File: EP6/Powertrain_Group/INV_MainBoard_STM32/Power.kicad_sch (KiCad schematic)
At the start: 42 parts, among them J3 LVBattery, U2 TPS5430DDA, U3 AMS1117-3.3

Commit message: Inverter board adjust
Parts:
- D3, D5: footprint Diode_SMD:D_SMB -> Diode_SMD:D_SOD-323
- U2: value TPS5430DDA -> TPS5430DDAR
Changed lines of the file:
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@@
 			)
 		)
-		(property "Footprint" "Diode_SMD:D_SMB"
+		(property "Footprint" "Diode_SMD:D_SOD-323"
 			(at 240.03 44.45 90)
 			(effects
@@
 			)
 		)
-		(property "Value" "TPS5430DDA"
+		(property "Value" "TPS5430DDAR"
 			(at 137.16 81.28 0)
 			(effects
@@
 			)
 		)
-		(property "Footprint" "Diode_SMD:D_SMB"
+		(property "Footprint" "Diode_SMD:D_SOD-323"
 			(at 264.16 93.98 90)
 			(effects

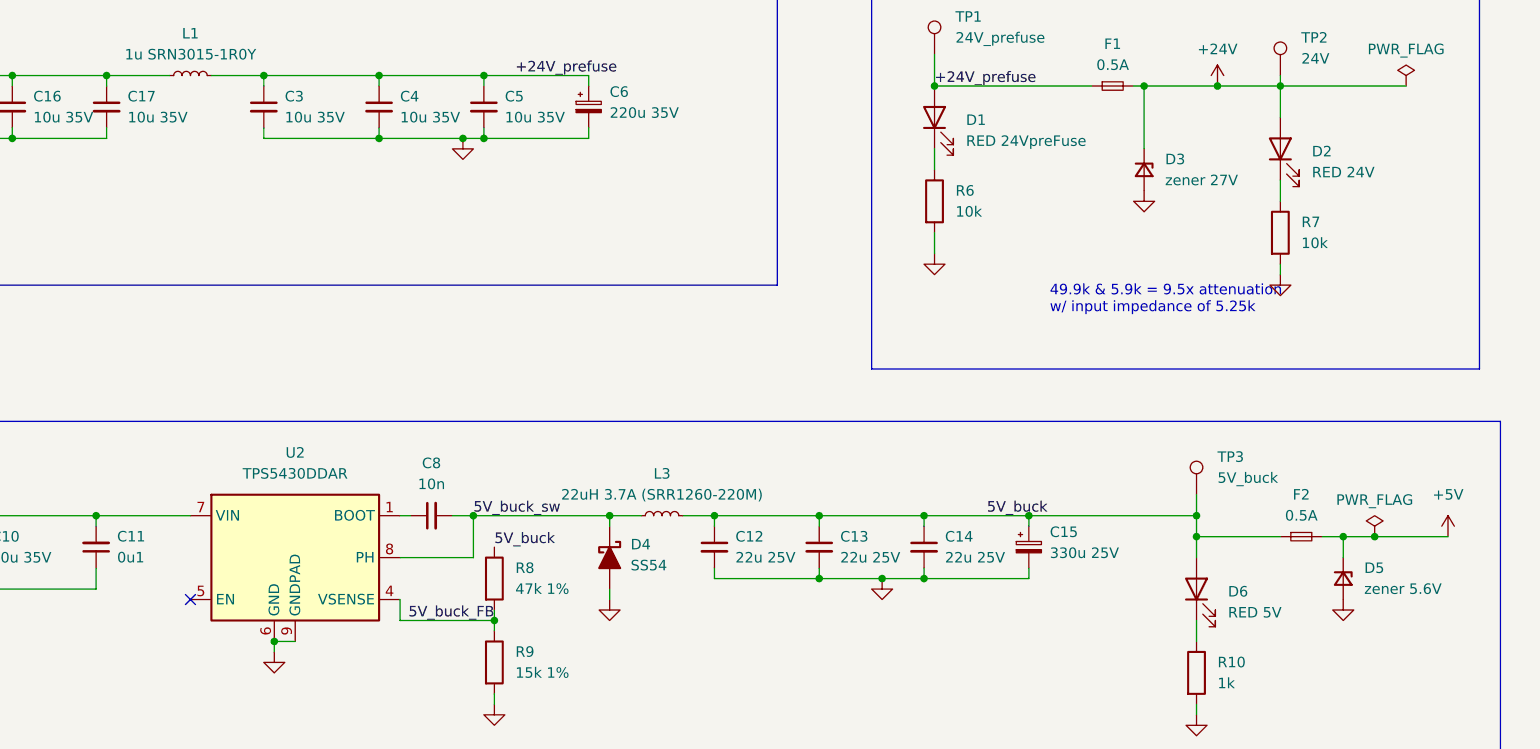
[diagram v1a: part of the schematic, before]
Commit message: batch update for JLCPCB 241117
6SBMS
ACC_HVLV1
INV_CurrentSense2
INV_CurrentSense3
DClinkCap1
INV_MainBoard_STM32
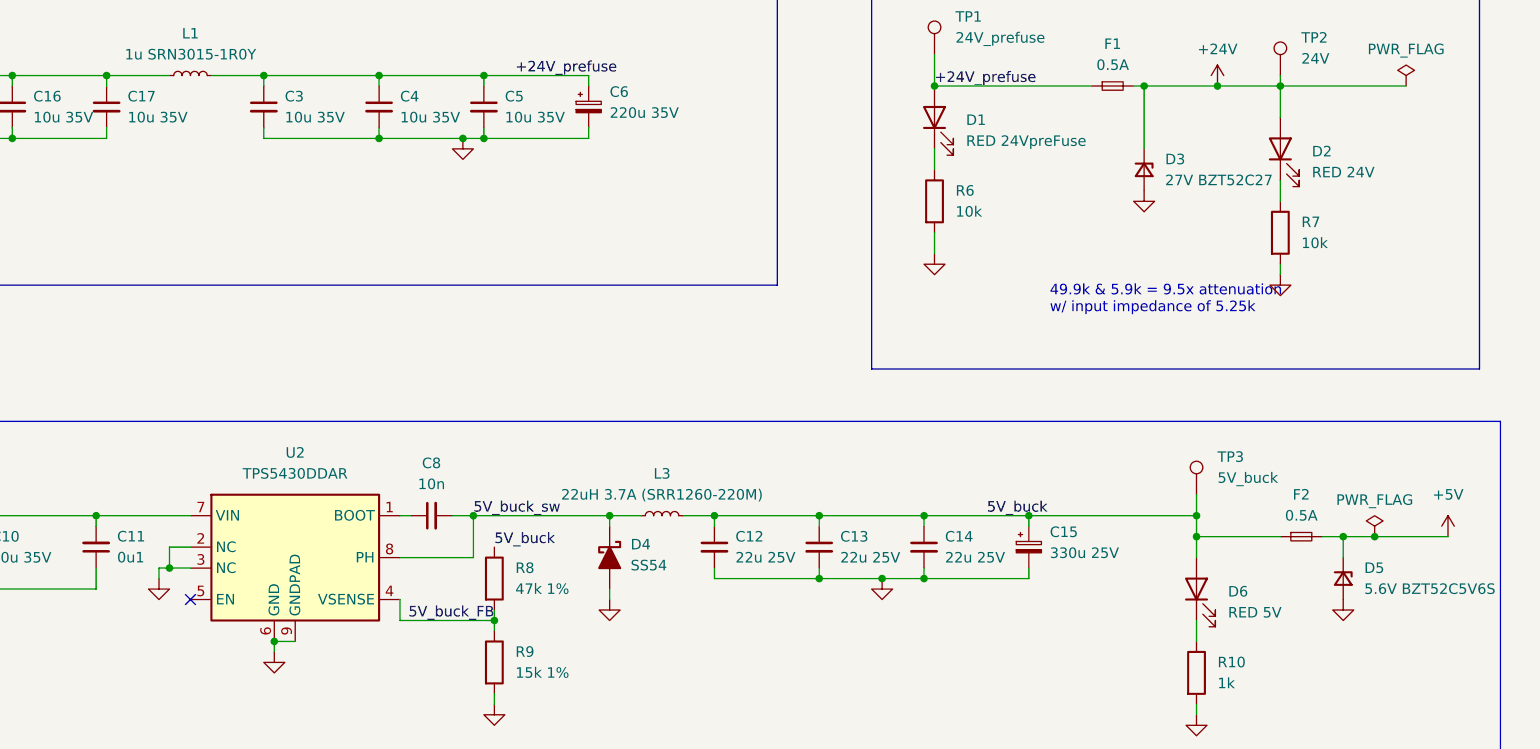
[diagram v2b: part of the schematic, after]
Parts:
- D3: value zener 27V -> 27V BZT52C27
- D4: footprint PCM_Diode_SMD_AKL:D_SMC -> Diode_SMD:D_SMA
- D5: value zener 5.6V -> 5.6V BZT52C5V6S
- U2: symbol Regulator_Switching:TPS5430DDA -> nturt_kicad_lib_EP6:TPS5430DDAR
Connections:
- net GND: now also U2.2 (NC), U2.3 (NC)
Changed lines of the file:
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@@
 	(title_block
 		(title "INV_MainBoard")
-		(date "2024-11-15")
-		(rev "1")
+		(date "2024-11-16")
+		(rev "1.0")
 		(company "NTURacing Team")
 		(comment 1 "郭哲明 Jack Kuo")
@@
 	)
 	(junction
+		(at 121.92 92.71)
+		(diameter 0)
+		(color 0 0 0 0)
+	)
+	(junction
 		(at 134.62 101.6)
 		(diameter 0)
@@
 	(wire
 		(pts
+			(xy 124.46 90.17) (xy 121.92 90.17)
+		)
+		(stroke
+			(width 0)
+			(type default)
+		)
+	)
+	(wire
+		(pts
 			(xy 78.74 45.72) (xy 82.55 45.72)
 		)
@@
 	(wire
 		(pts
+			(xy 121.92 92.71) (xy 124.46 92.71)
+		)
+		(stroke
+			(width 0)
+			(type default)
+		)
+	)
+	(wire
+		(pts
 			(xy 63.5 30.48) (xy 82.55 30.48)
 		)
@@
 	(wire
 		(pts
+			(xy 120.65 93.98) (xy 120.65 92.71)
+		)
+		(stroke
+			(width 0)
+			(type default)
+		)
+	)
+	(wire
+		(pts
 			(xy 256.54 34.29) (xy 256.54 38.1)
 		)
@@
 	(wire
 		(pts
+			(xy 120.65 92.71) (xy 121.92 92.71)
+		)
+		(stroke
+			(width 0)
+			(type default)
+		)
+	)
+	(wire
+		(pts
 			(xy 161.29 99.06) (xy 149.86 99.06)
 		)
@@
 	(wire
 		(pts
+			(xy 121.92 90.17) (xy 121.92 92.71)
+		)
+		(stroke
+			(width 0)
+			(type default)
+		)
+	)
+	(wire
+		(pts
 			(xy 133.35 33.02) (xy 147.32 33.02)
 		)
@@
 			)
 		)
-		(property "Footprint" "PCM_Diode_SMD_AKL:D_SMC"
+		(property "Footprint" "Diode_SMD:D_SMA"
 			(at 175.26 91.44 0)
 			(effects
@@
 		(fields_autoplaced yes)
 		(property "Reference" "D3"
-			(at 242.57 43.1799 90)
+			(at 242.57 43.18 90)
 			(effects
 				(font
@@
 			)
 		)
-		(property "Value" "zener 27V"
-			(at 242.57 45.7199 90)
+		(property "Value" "27V BZT52C27"
+			(at 242.57 45.72 90)
 			(effects
 				(font
@@
 	)
 	(symbol
-		(lib_id "Regulator_Switching:TPS5430DDA")
+		(lib_id "nturt_kicad_lib_EP6:TPS5430DDAR")
 		(at 137.16 91.44 0)
 		(unit 1)
@@
 			)
 		)
-		(property "Value" "zener 5.6V"
+		(property "Value" "5.6V BZT52C5V6S"
 			(at 266.7 95.25 90)
 			(effects
@@
 					(unit 1)
 				)
+			)
+		)
+	)
+	(symbol
+		(lib_id "power:GND")
+		(at 120.65 93.98 0)
+		(unit 1)
+		(exclude_from_sim no)
+		(in_bom yes)
+		(on_board yes)
+		(dnp no)
+		(fields_autoplaced yes)
+		(property "Reference" "#PWR019"
+			(at 120.65 100.33 0)
+			(effects
+				(font
+					(size 1.27 1.27)
+				)
+				(hide yes)
+			)
+		)
+		(property "Value" "GND"
+			(at 120.65 99.06 0)
+			(effects
+				(font
+					(size 1.27 1.27)
+				)
+				(hide yes)
+			)
+		)
+		(property "Footprint" ""
+			(at 120.65 93.98 0)
+			(effects
+				(font
+					(size 1.27 1.27)
+				)
+				(hide yes)
+			)
+		)
+		(property "Datasheet" ""
+			(at 120.65 93.98 0)
+			(effects
+				(font
+					(size 1.27 1.27)
+				)
+				(hide yes)
+			)
+		)
+		(property "Description" "Power symbol creates a global label with name \"GND\" , ground"
+			(at 120.65 93.98 0)
+			(effects
+				(font
+					(size 1.27 1.27)
+				)
+				(hide yes)
+			)
+		)
+		(pin "1"
+		)
+		(instances
+			(project "INV_MainBoard_STM32"
+				(path "/963ad98e-e494-4953-a7e0-8b20a365a35d/1fbe31ff-2616-447c-a0f3-fc1e6c14e58b"
+					(reference "#PWR019")
+					(unit 1)
+				)

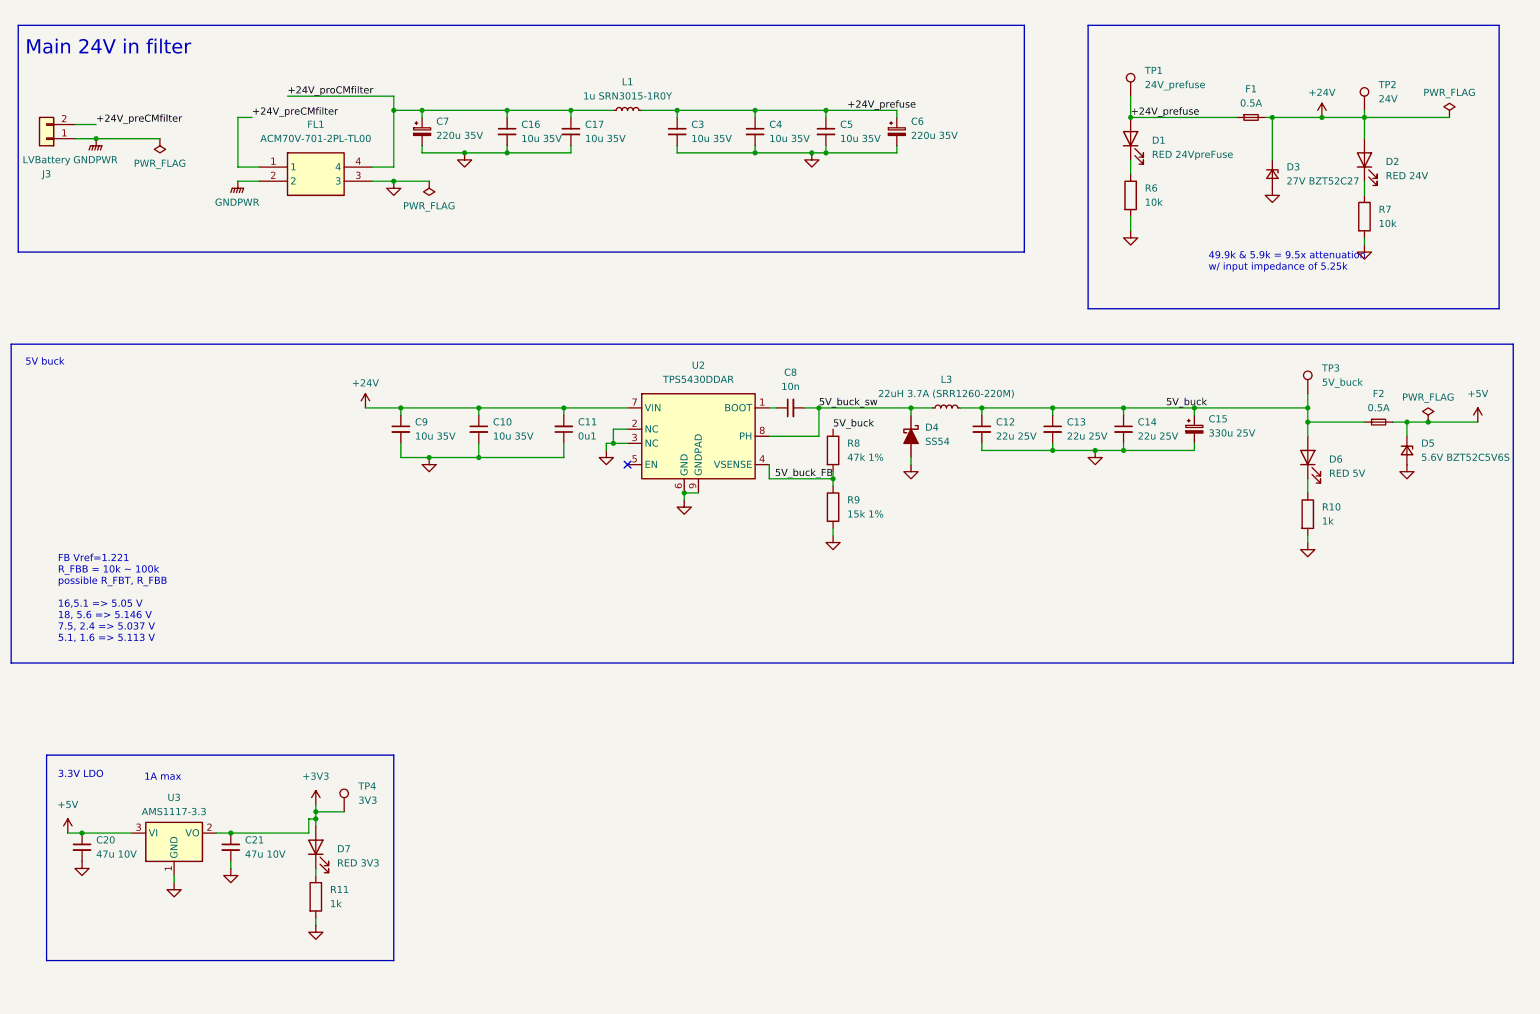
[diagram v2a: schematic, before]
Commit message: update INV_MainBoard_STM32 to V2.0
big update to match new INV_GateDriver
and use H743ZI as MCU
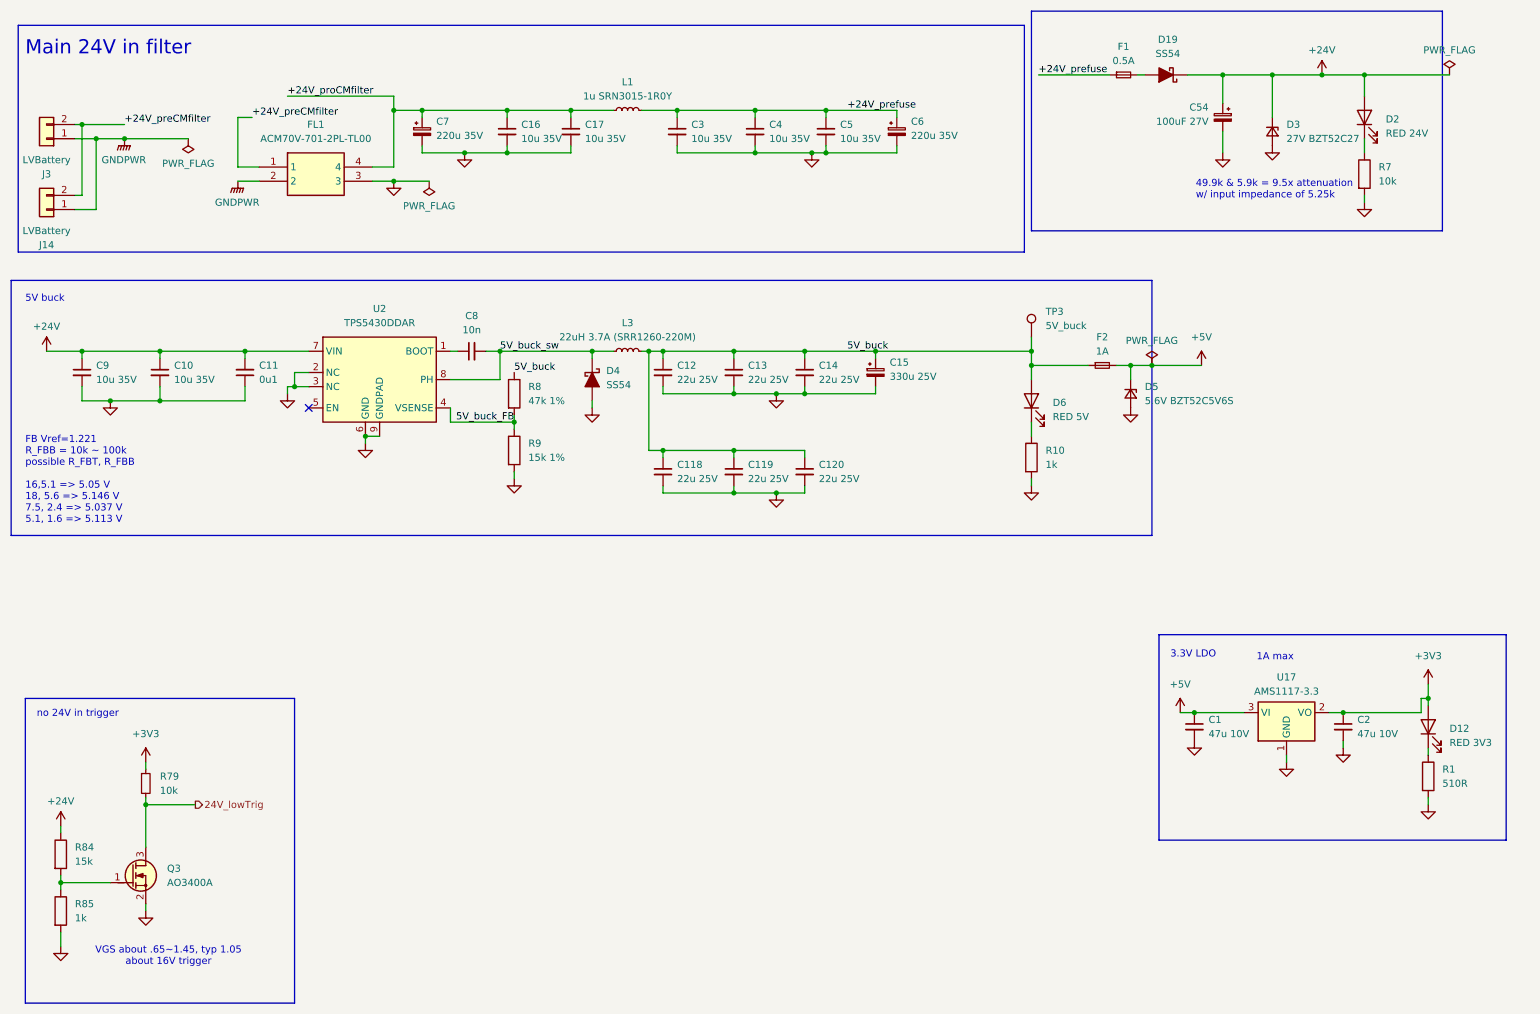
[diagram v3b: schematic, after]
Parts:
- removed C20, C21: 47u 10V, Capacitor_SMD:C_1206_3216Metric, symbol Device:C_Small
- removed D1: RED 24VpreFuse, LED_SMD:LED_0603_1608Metric, symbol Device:LED
- removed D7: RED 3V3, LED_SMD:LED_0603_1608Metric, symbol Device:LED
- removed R11: 1k, Resistor_SMD:R_0402_1005Metric, symbol Device:R
- removed R6: 10k, Resistor_SMD:R_0402_1005Metric, symbol Device:R
- removed TP1: 24V_prefuse, TestPoint:TestPoint_Pad_D1.0mm, symbol Connector:TestPoint
- removed TP2: 24V, TestPoint:TestPoint_Pad_D1.0mm, symbol Connector:TestPoint
- removed TP4: 3V3, TestPoint:TestPoint_Pad_D1.0mm, symbol Connector:TestPoint
- removed U3: AMS1117-3.3, Package_TO_SOT_SMD:SOT-223-3_TabPin2, symbol Regulator_Linear:AMS1117-3.3
- added C1, C2: 47u 10V, Capacitor_SMD:C_1206_3216Metric, symbol Device:C_Small
- added C118, C119, C120: 22u 25V, Capacitor_SMD:C_1206_3216Metric, symbol Device:C_Small
- added C54: 100uF 27V, Capacitor_THT:CP_Radial_D10.0mm_P5.00mm, symbol Device:C_Polarized_Small
- added D12: RED 3V3, LED_SMD:LED_0603_1608Metric, symbol Device:LED
- added D19: SS54, Diode_SMD:D_SMA, symbol PCM_Diode_Schottky_AKL:SS54
- added J14: LVBattery, Connector_JST:JST_VH_B2P-VH_1x02_P3.96mm_Vertical, symbol Connector_Generic:Conn_01x02
- added Q3: AO3400A, Package_TO_SOT_SMD:SOT-23, symbol PCM_Transistor_MOSFET_AKL:AO3400A
- added R1: 510R, Resistor_SMD:R_0402_1005Metric, symbol Device:R
- added R79: 10k, Resistor_SMD:R_0402_1005Metric, symbol Device:R_Small
- added R84: 15k, Resistor_SMD:R_0402_1005Metric, symbol Device:R
- added R85: 1k, Resistor_SMD:R_0402_1005Metric, symbol Device:R
- added U17: AMS1117-3.3, Package_TO_SOT_SMD:SOT-223-3_TabPin2, symbol Regulator_Linear:AMS1117-3.3
- F1: footprint Fuse:Fuse_2512_6332Metric_Pad1.52x3.35mm_HandSolder -> Fuse:Fuse_1206_3216Metric
- F2: value 0.5A -> 1A; footprint Fuse:Fuse_2512_6332Metric_Pad1.52x3.35mm_HandSolder -> Fuse:Fuse_1206_3216Metric
- J3: footprint Connector_JST:JST_XH_B2B-XH-A_1x02_P2.50mm_Vertical -> Connector_JST:JST_VH_B2P-VH_1x02_P3.96mm_Vertical
- L3: footprint SamacSys_Parts:SRR1260A220M -> SamacSys_Parts_EP6:SRR1260A220M
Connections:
- net +24V: now also C54.1, D19.1 (K), R84.1; no longer F1.2
- net +24V_preCMfilter: now also J14.2 (Pin_2)
- net +3V3: now also C2.1, D12.2 (A), R79.1, U17.2 (VO)
- net +5V: now also C1.1, U17.3 (VI)
- net 5V_buck: now also C118.1, C119.1, C120.1
- net GND: now also C1.2, C118.2, C119.2, C120.2, C2.2, C54.2, Q3.2 (S), R1.2, R85.2, U17.1 (GND)
- net GNDPWR: now also J14.1 (Pin_1)
- new net: D19.2 (A), F1.2
- new net: Q3.1 (G), R84.2, R85.1
- new net: D12.1 (K), R1.1
- new net 24V_lowTrig: Q3.3 (D), R79.2
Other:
- note added: "VGS about .65~1.45, typ 1.05 about 16V trigger"
- note added: "no 24V in trigger"
- title: INV_MainBoard -> INV_MainBoard_STM32
- moved on the sheet: C10, C11, C12, C13, C14, C15, C8, C9, D2, D3, D4, D5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

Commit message: update INV_MainBoard_STM32 to V2.1
update for JLCPCB, include change in 1.65 Vref and some name change for easier JLCPCBA BOM selection
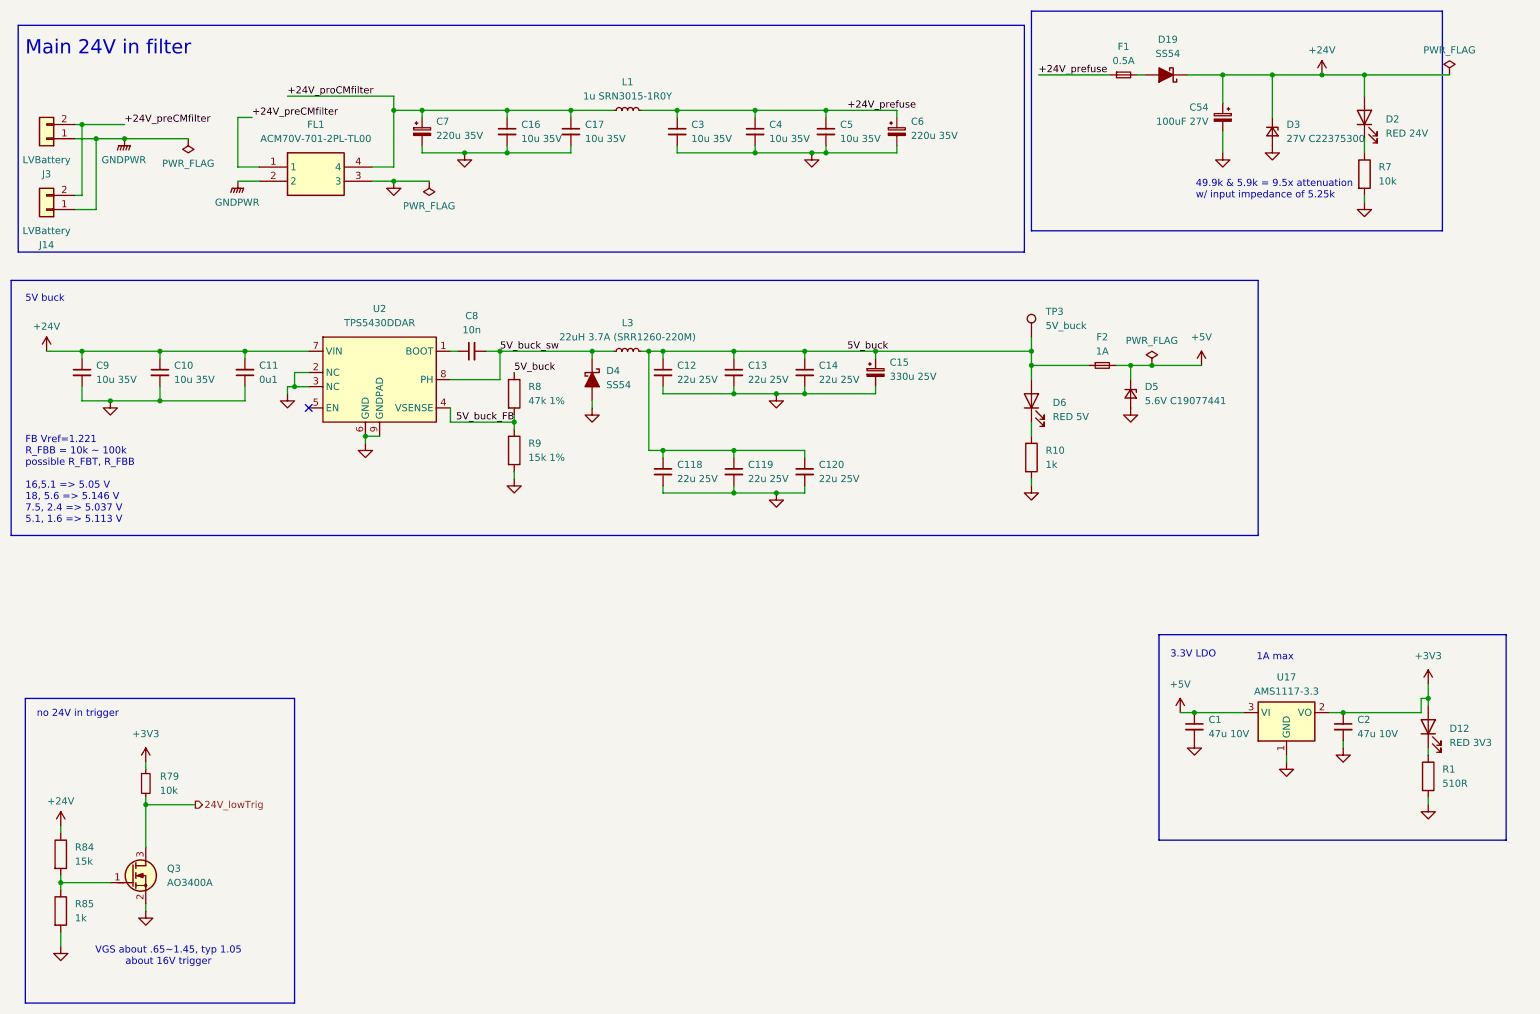
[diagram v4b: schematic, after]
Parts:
- D3: value 27V BZT52C27 -> 27V C22375300
- D5: value 5.6V BZT52C5V6S -> 5.6V C19077441
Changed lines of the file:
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@@
 	(title_block
 		(title "INV_MainBoard_STM32")
-		(rev "2.0")
+		(date "2025-02-28")
+		(rev "2.1")
 		(company "NTURacing Team")
 		(comment 1 "郭哲明 Jack Kuo")
@@
 	(rectangle
 		(start 13.97 63.5)
-		(end 218.44 109.22)
+		(end 237.49 109.22)
 		(stroke
 			(width 0)
@@
 			)
 		)
-		(property "Value" "27V BZT52C27"
+		(property "Value" "27V C22375300"
 			(at 242.57 38.1 90)
 			(effects
@@
 			)
 		)
-		(property "Value" "5.6V BZT52C5V6S"
+		(property "Value" "5.6V C19077441"
 			(at 217.17 85.09 90)
 			(effects
